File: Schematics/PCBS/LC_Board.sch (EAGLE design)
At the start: 24 parts, among them IC1 ATMEGA328P-AU, Q10 220mA/50V/3.5Ω, U1 LT1763CS8-3.3#TRPBF

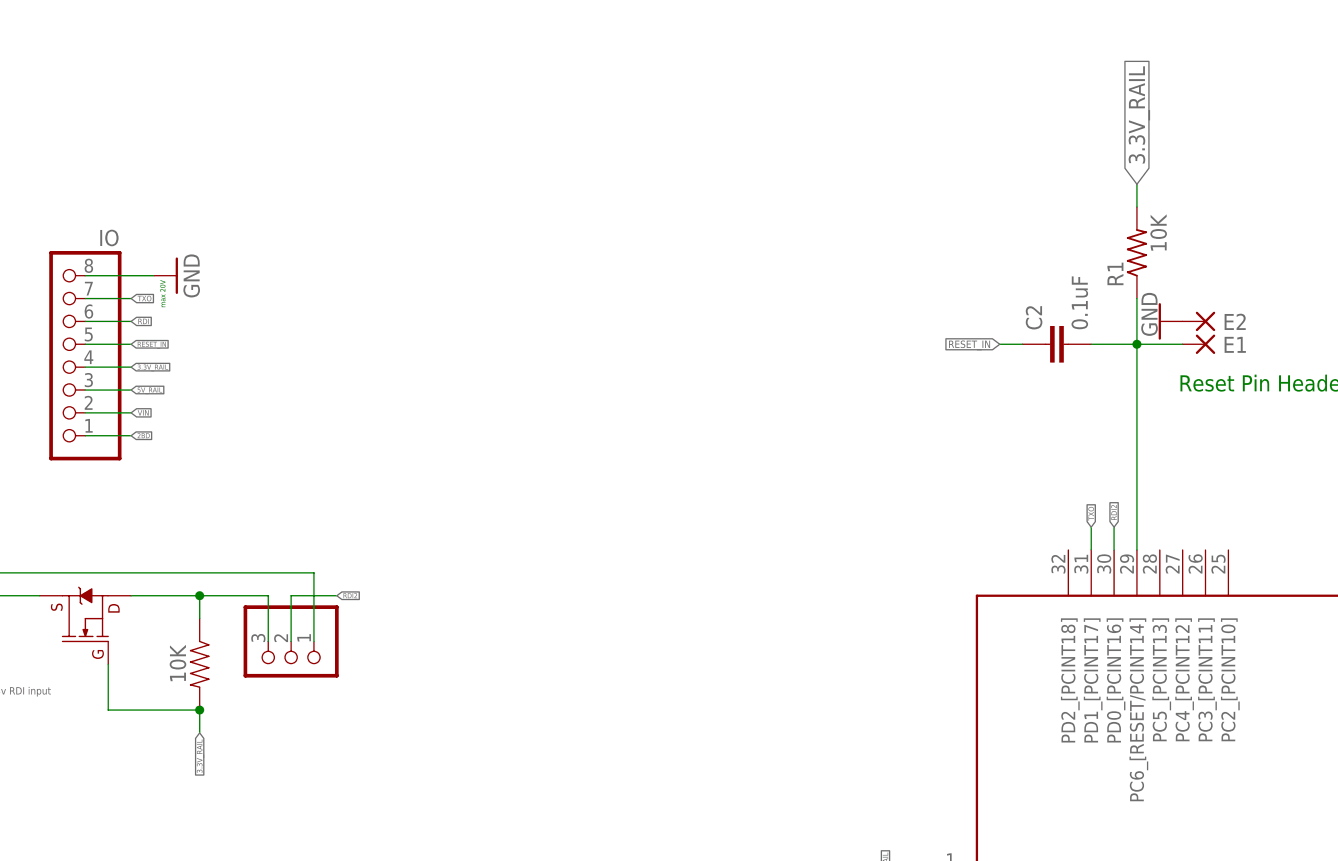
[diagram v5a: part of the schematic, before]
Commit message: PCB layout fixed
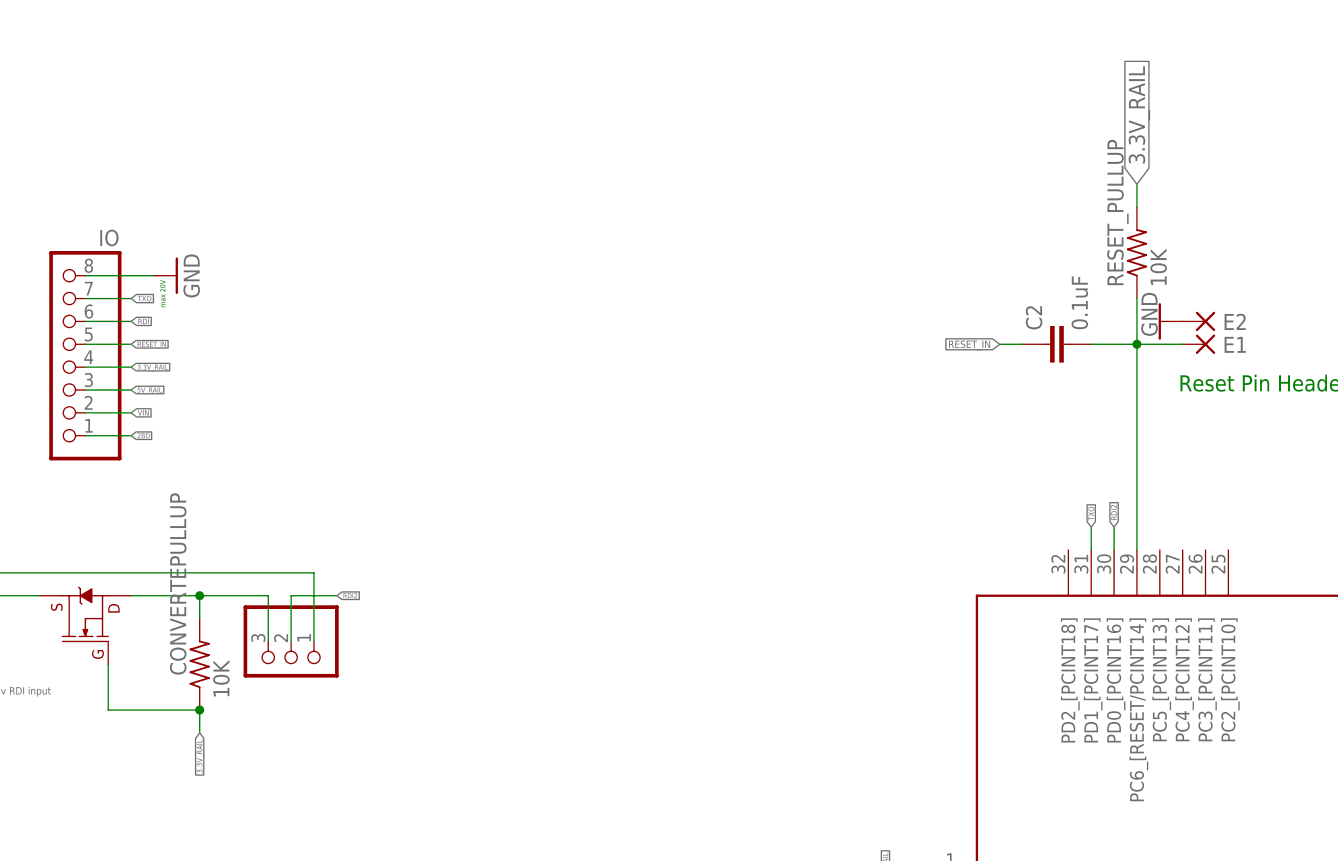
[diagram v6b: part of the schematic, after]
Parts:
- removed R1: 10K, adafruit:R-US_0207/10
- removed R3: 10K, SparkFun-Resistors:10OHM-HORIZ-1/4W-1%
- added CONVERTEPULLUP: 10K, audio amplifier example:R-US_R0603
- added RESET_PULLUP: 10K, audio amplifier example:R-US_R0402
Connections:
- net 3.3V_RAIL: now also CONVERTEPULLUP.1, RESET_PULLUP.2; no longer R1.2, R3.2
- net N$15: now also RESET_PULLUP.1; no longer R1.1
- net RXI2: now also CONVERTEPULLUP.2; no longer R3.1
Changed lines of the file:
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@@
 <layer number="154" name="FabDoc2" color="7" fill="1" visible="yes" active="yes"/>
 <layer number="155" name="FabDoc3" color="7" fill="1" visible="yes" active="yes"/>
+<layer number="166" name="AntennaArea" color="7" fill="1" visible="yes" active="yes"/>
+<layer number="168" name="4mmHeightArea" color="7" fill="1" visible="yes" active="yes"/>
 <layer number="191" name="mNets" color="7" fill="1" visible="yes" active="yes"/>
 <layer number="192" name="mBusses" color="7" fill="1" visible="yes" active="yes"/>
@@
 <part name="GND11" library="supply1" library_urn="urn:adsk.eagle:library:371" deviceset="GND" device=""/>
 <part name="GND16" library="supply1" library_urn="urn:adsk.eagle:library:371" deviceset="GND" device=""/>
-<part name="R1" library="adafruit" library_urn="urn:adsk.eagle:library:420" deviceset="R-US_" device="0207/10" package3d_urn="urn:adsk.eagle:package:6240597/1" value="10K"/>
 <part name="GND17" library="supply1" library_urn="urn:adsk.eagle:library:371" deviceset="GND" device=""/>
 <part name="GND18" library="supply1" library_urn="urn:adsk.eagle:library:371" deviceset="GND" device=""/>
-<part name="R3" library="SparkFun-Resistors" deviceset="10OHM" device="-HORIZ-1/4W-1%" value="10K"/>
 <part name="Q10" library="SparkFun-DiscreteSemi" deviceset="MOSFET-NCH" device="-BSS138" value="220mA/50V/3.5Ω"/>
 <part name="E1" library="52101-101-REV-A" library_urn="urn:adsk.eagle:library:15662110" deviceset="DPADS_PAD" device="-0400-S" package3d_urn="urn:adsk.eagle:package:15662248/2"/>
@@
 <part name="JP2" library="pinhead" library_urn="urn:adsk.eagle:library:325" deviceset="PINHD-1X3" device="" package3d_urn="urn:adsk.eagle:package:22458/2" value="switching from 5v RDI to 3.3v RDI input"/>
 <part name="JP3" library="pinhead" library_urn="urn:adsk.eagle:library:325" deviceset="PINHD-1X3" device="" package3d_urn="urn:adsk.eagle:package:22458/2"/>
+<part name="CONVERTEPULLUP" library="audio amplifier example" library_urn="urn:adsk.eagle:library:970892" deviceset="R-US_" device="R0603" package3d_urn="urn:adsk.eagle:package:970938/2" value="10K"/>
+<part name="RESET_PULLUP" library="audio amplifier example" library_urn="urn:adsk.eagle:library:970892" deviceset="R-US_" device="R0402" package3d_urn="urn:adsk.eagle:package:970935/2" value="10K"/>
+<part name="FRAME1" library="frames" library_urn="urn:adsk.eagle:library:229" deviceset="A3L-LOC" device=""/>
 </parts>
 <sheets>
@@
 <attribute name="VALUE" x="542.28" y="-29.04" size="1.016" layer="96" rot="R270"/>
 </instance>
-<instance part="R1" gate="G$1" x="568.96" y="43.18" smashed="yes" rot="R90">
-<attribute name="NAME" x="567.4614" y="39.37" size="1.778" layer="95" rot="R90"/>
-<attribute name="VALUE" x="572.262" y="43.18" size="1.778" layer="96" rot="R90"/>
-</instance>
 <instance part="GND17" gate="1" x="571.5" y="35.56" smashed="yes" rot="R270">
 <attribute name="VALUE" x="569.468" y="38.862" size="1.778" layer="96" rot="R270"/>
@@
 <instance part="GND18" gate="1" x="462.28" y="40.64" smashed="yes" rot="R90">
 <attribute name="VALUE" x="464.82" y="38.1" size="1.778" layer="96" rot="R90"/>
-</instance>
-<instance part="R3" gate="G$1" x="464.82" y="-2.54" smashed="yes" rot="R270">
-<attribute name="VALUE" x="463.296" y="-2.54" size="1.778" layer="96" font="vector" rot="R270" align="top-center"/>
 </instance>
 <instance part="Q10" gate="NMOS" x="452.12" y="2.54" smashed="yes" rot="R90"/>
@@
 <instance part="JP3" gate="A" x="474.98" y="-2.54" smashed="yes" rot="R270">
 <attribute name="VALUE" x="467.36" y="3.81" size="1.778" layer="96" rot="R270"/>
+</instance>
+<instance part="CONVERTEPULLUP" gate="G$1" x="464.82" y="-2.54" smashed="yes" rot="R90">
+<attribute name="NAME" x="463.3214" y="-3.81" size="1.778" layer="95" rot="R90"/>
+<attribute name="VALUE" x="468.122" y="-6.35" size="1.778" layer="96" rot="R90"/>
+</instance>
+<instance part="RESET_PULLUP" gate="G$1" x="568.96" y="43.18" smashed="yes" rot="R90">
+<attribute name="NAME" x="567.4614" y="39.37" size="1.778" layer="95" rot="R90"/>
+<attribute name="VALUE" x="572.262" y="39.37" size="1.778" layer="96" rot="R90"/>
+</instance>
+<instance part="FRAME1" gate="G$1" x="381" y="-187.96" smashed="yes">
+<attribute name="DRAWING_NAME" x="725.17" y="-172.72" size="2.54" layer="94"/>
+<attribute name="LAST_DATE_TIME" x="725.17" y="-177.8" size="2.286" layer="94"/>
+<attribute name="SHEET" x="738.505" y="-182.88" size="2.54" layer="94"/>
 </instance>
 </instances>
@@
 </segment>
 <segment>
-<pinref part="R1" gate="G$1" pin="2"/>
 <wire x1="568.96" y1="48.26" x2="568.96" y2="50.8" width="0.1524" layer="91"/>
 <label x="568.96" y="50.8" size="1.778" layer="95" rot="R90" xref="yes"/>
-</segment>
-<segment>
-<pinref part="R3" gate="G$1" pin="2"/>
+<pinref part="RESET_PULLUP" gate="G$1" pin="2"/>
+</segment>
+<segment>
 <label x="464.82" y="-10.16" size="0.6096" layer="95" rot="R270" xref="yes"/>
 <wire x1="464.82" y1="-7.62" x2="464.82" y2="-10.16" width="0.1524" layer="91"/>
@@
 <wire x1="454.66" y1="-2.54" x2="454.66" y2="-7.62" width="0.1524" layer="91"/>
 <wire x1="454.66" y1="-7.62" x2="464.82" y2="-7.62" width="0.1524" layer="91"/>
+<pinref part="CONVERTEPULLUP" gate="G$1" pin="1"/>
 <junction x="464.82" y="-7.62"/>
 </segment>
@@
 <net name="N$15" class="0">
 <segment>
-<pinref part="R1" gate="G$1" pin="1"/>
 <wire x1="568.96" y1="10.16" x2="568.96" y2="33.02" width="0.1524" layer="91"/>
 <wire x1="568.96" y1="33.02" x2="568.96" y2="38.1" width="0.1524" layer="91"/>
@@
 <wire x1="568.96" y1="33.02" x2="563.88" y2="33.02" width="0.1524" layer="91"/>
 <pinref part="C2" gate="G$1" pin="2"/>
+<pinref part="RESET_PULLUP" gate="G$1" pin="1"/>
 </segment>
 </net>
@@
 <net name="RXI2" class="0">
 <segment>
-<pinref part="R3" gate="G$1" pin="1"/>
 <wire x1="457.2" y1="5.08" x2="464.82" y2="5.08" width="0.1524" layer="91"/>
 <wire x1="464.82" y1="5.08" x2="464.82" y2="2.54" width="0.1524" layer="91"/>
@@
 <pinref part="JP3" gate="A" pin="3"/>
 <wire x1="472.44" y1="5.08" x2="472.44" y2="0" width="0.1524" layer="91"/>
-</segment>
-</net>
+<pinref part="CONVERTEPULLUP" gate="G$1" pin="2"/>
+</segment>
+</net>

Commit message: updated Reset_pull footprint to 603 from 403
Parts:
- RESET_PULLUP: device audio amplifier example:R-US_R0402 -> audio amplifier example:R-US_R0603
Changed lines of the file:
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@@
 <part name="JP3" library="pinhead" library_urn="urn:adsk.eagle:library:325" deviceset="PINHD-1X3" device="" package3d_urn="urn:adsk.eagle:package:22458/2"/>
 <part name="CONVERTEPULLUP" library="audio amplifier example" library_urn="urn:adsk.eagle:library:970892" deviceset="R-US_" device="R0603" package3d_urn="urn:adsk.eagle:package:970938/2" value="10K"/>
-<part name="RESET_PULLUP" library="audio amplifier example" library_urn="urn:adsk.eagle:library:970892" deviceset="R-US_" device="R0402" package3d_urn="urn:adsk.eagle:package:970935/2" value="10K"/>
 <part name="FRAME1" library="frames" library_urn="urn:adsk.eagle:library:229" deviceset="A3L-LOC" device=""/>
+<part name="RESET_PULLUP" library="audio amplifier example" library_urn="urn:adsk.eagle:library:970892" deviceset="R-US_" device="R0603" package3d_urn="urn:adsk.eagle:package:970938/2" value="10K"/>
 </parts>
 <sheets>
@@
 <attribute name="VALUE" x="468.122" y="-6.35" size="1.778" layer="96" rot="R90"/>
 </instance>
-<instance part="RESET_PULLUP" gate="G$1" x="568.96" y="43.18" smashed="yes" rot="R90">
-<attribute name="NAME" x="567.4614" y="39.37" size="1.778" layer="95" rot="R90"/>
-<attribute name="VALUE" x="572.262" y="39.37" size="1.778" layer="96" rot="R90"/>
-</instance>
 <instance part="FRAME1" gate="G$1" x="381" y="-187.96" smashed="yes">
 <attribute name="DRAWING_NAME" x="725.17" y="-172.72" size="2.54" layer="94"/>
@@
 <attribute name="SHEET" x="738.505" y="-182.88" size="2.54" layer="94"/>
 </instance>
+<instance part="RESET_PULLUP" gate="G$1" x="568.96" y="43.18" smashed="yes" rot="R90">
+<attribute name="NAME" x="567.4614" y="39.37" size="1.778" layer="95" rot="R90"/>
+<attribute name="VALUE" x="572.262" y="39.37" size="1.778" layer="96" rot="R90"/>
+</instance>
 </instances>

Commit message: routing for PCB 1  ok outcome
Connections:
- net N$1 renamed RED1
- net N$15 renamed RESET_LINE
- net N$2 renamed GREEN1
- net N$3 renamed BLUE1
- net N$4 renamed RED2
- net N$5 renamed GREEN2
- net N$6 renamed BLUE2
- net N$7 renamed RED3
- net N$8 renamed GREEN3
- net N$9 renamed BLUE3
